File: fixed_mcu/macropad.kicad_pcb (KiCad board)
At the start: 2 copper layers, 92.3 x 115.3 mm, 120 parts, among them J1 USB_C_Receptacle_USB2.0_16P, J2 Conn_01x02, J3 Conn_01x04_Socket, SW1 CherryMX, SW10 CherryMX, SW11 CherryMX, SW12 CherryMX, SW13 CherryMX, SW14 CherryMX, SW15 CherryMX, SW16 CherryMX, SW17 CherryMX, SW18 CherryMX, SW19 CherryMX, SW2 CherryMX, SW20 CherryMX, SW21 SW_Push, SW3 CherryMX, SW4 CherryMX, SW5 CherryMX, SW6 CherryMX, SW7 CherryMX, SW8 CherryMX, SW9 CherryMX, U1 NCP1117-3.3_SOT223, U2 RP2040, U3 SRV05-4, U4 W25Q128JVS, U5 74AHCT1G125, Y1 Crystal_GND24

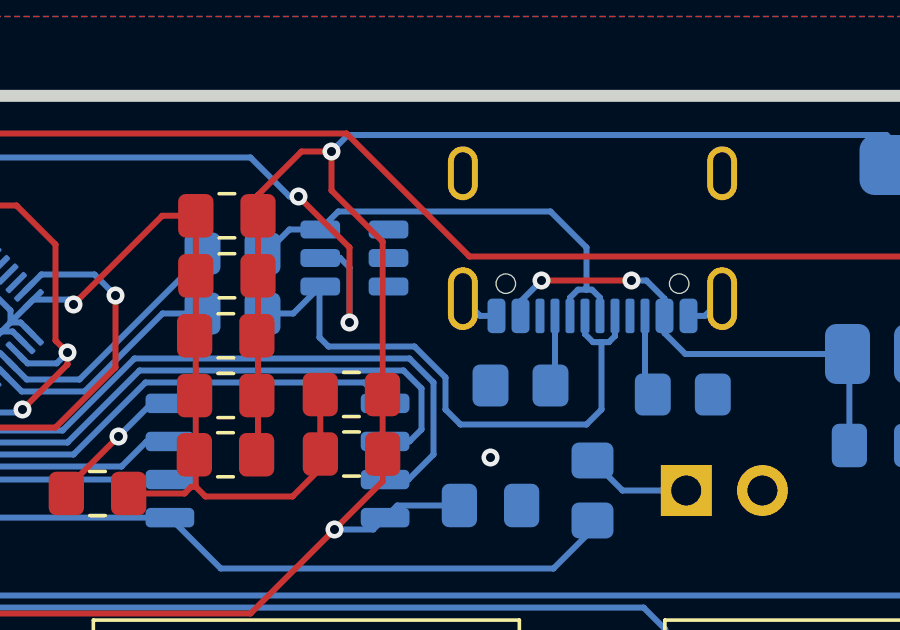
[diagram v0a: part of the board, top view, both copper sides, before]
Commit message: finished modeling enclosures and pad
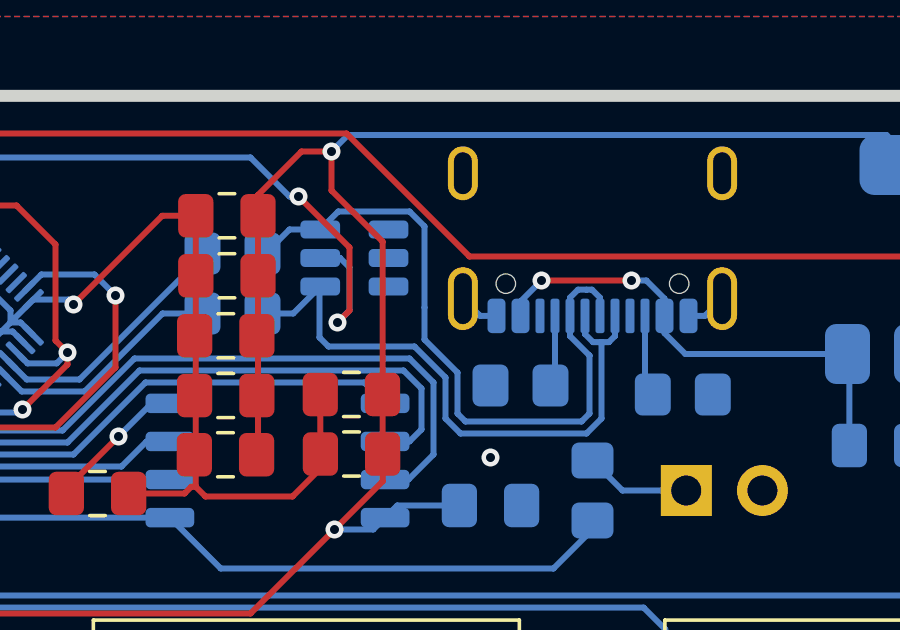
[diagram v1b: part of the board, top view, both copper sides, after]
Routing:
- net /MCU/USB_D-: track 15.8 -> 23.5 mm
- net /MCU/USB_D+: track 20.2 -> 20.8 mm
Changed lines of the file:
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@@
-	)
-	(segment
-		(start 71.9 47.3)
-		(end 73.6 49)
-		(width 0.2)
-		(layer "F.Cu")
-		(net "+5V")
 	)
 	(segment
@@
 	)
 	(segment
+		(start 73.6 49)
+		(end 71.9 47.3)
+		(width 0.2)
+		(layer "F.Cu")
+		(net "+5V")
+	)
+	(segment
+		(start 73.2 51.5)
+		(end 73.6 51.1)
+		(width 0.2)
+		(layer "F.Cu")
+		(net "+5V")
+	)
+	(segment
 		(start 54.9 97.2)
 		(end 73.9 97.2)
@@
 	)
 	(segment
-		(start 73.6 49)
-		(end 73.6 51.5)
-		(width 0.2)
-		(layer "F.Cu")
-		(net "+5V")
-	)
-	(segment
 		(start 54.8 135.3)
 		(end 46.1 135.3)
@@
 		(net "+5V")
 	)
+	(segment
+		(start 73.6 51.1)
+		(end 73.6 49)
+		(width 0.2)
+		(layer "F.Cu")
+		(net "+5V")
+	)
 	(via
 		(at 92.8 135.3)
@@
 	)
 	(via
-		(at 73.6 51.5)
+		(at 73.2 51.5)
 		(size 0.6)
 		(drill 0.3)
@@
 		(drill 0.3)
 		(layers "F.Cu" "B.Cu")
+		(net "+5V")
+	)
+	(segment
+		(start 73.287499 49.35)
+		(end 72.625 49.35)
+		(width 0.2)
+		(layer "B.Cu")
 		(net "+5V")
 	)
@@
 	)
 	(segment
+		(start 73.6 51.1)
+		(end 73.6 49.662501)
+		(width 0.2)
+		(layer "B.Cu")
+		(net "+5V")
+	)
+	(segment
 		(start 74.8875 150.55)
 		(end 74.8875 151.1125)
@@
 	(segment
 		(start 73.6 49.662501)
-		(end 73.6 51.5)
+		(end 73.287499 49.35)
 		(width 0.2)
 		(layer "B.Cu")
@@
 	)
 	(segment
+		(start 73.2 51.5)
+		(end 73.6 51.1)
+		(width 0.2)
+		(layer "B.Cu")
+		(net "+5V")
+	)
+	(segment
 		(start 92.35 77.55)
 		(end 92.35 76.7)
@@
 	)
 	(segment
-		(start 72.625 49.35)
-		(end 73.287499 49.35)
-		(width 0.2)
-		(layer "B.Cu")
-		(net "+5V")
-	)
-	(segment
 		(start 92.25 115.65)
 		(end 92.25 114.8)
@@
 	)
 	(segment
-		(start 73.287499 49.35)
-		(end 73.6 49.662501)
-		(width 0.2)
-		(layer "B.Cu")
-		(net "+5V")
-	)
-	(segment
 		(start 112.9875 93.9625)
 		(end 111.3 95.65)
@@
 	)
 	(segment
+		(start 75.765686 52.3)
+		(end 72.9 52.3)
+		(width 0.2)
+		(layer "B.Cu")
+		(net "/MCU/USB_D+")
+	)
+	(segment
 		(start 81.45 51.88741)
 		(end 81.71759 52.155)
@@
 	)
 	(segment
-		(start 82 54.4)
-		(end 81.5 54.9)
-		(width 0.2)
-		(layer "B.Cu")
-		(net "/MCU/USB_D+")
-	)
-	(segment
-		(start 75.765686 52.3)
-		(end 72.9 52.3)
-		(width 0.2)
-		(layer "B.Cu")
-		(net "/MCU/USB_D+")
-	)
-	(segment
-		(start 76.8 54.4)
-		(end 76.8 53.334314)
-		(width 0.2)
-		(layer "B.Cu")
-		(net "/MCU/USB_D+")
-	)
-	(segment
 		(start 82.245 52.155)
 		(end 82.45 51.95)
@@
 	)
 	(segment
-		(start 82 52.155)
-		(end 82 54.4)
-		(width 0.2)
-		(layer "B.Cu")
-		(net "/MCU/USB_D+")
-	)
-	(segment
-		(start 81.5 54.9)
-		(end 77.3 54.9)
+		(start 76.8 54.7)
+		(end 76.8 53.334314)
+		(width 0.2)
+		(layer "B.Cu")
+		(net "/MCU/USB_D+")
+	)
+	(segment
+		(start 82 54.7)
+		(end 81.5 55.2)
 		(width 0.2)
 		(layer "B.Cu")
@@
 	)
 	(segment
+		(start 82 52.155)
+		(end 82 54.7)
+		(width 0.2)
+		(layer "B.Cu")
+		(net "/MCU/USB_D+")
+	)
+	(segment
+		(start 72.6 52)
+		(end 72.6 50.325)
+		(width 0.2)
+		(layer "B.Cu")
+		(net "/MCU/USB_D+")
+	)
+	(segment
+		(start 82 52.155)
+		(end 82.245 52.155)
+		(width 0.2)
+		(layer "B.Cu")
+		(net "/MCU/USB_D+")
+	)
+	(segment
+		(start 72.6 50.325)
+		(end 72.625 50.3)
+		(width 0.2)
+		(layer "B.Cu")
+		(net "/MCU/USB_D+")
+	)
+	(segment
 		(start 72.9 52.3)
 		(end 72.6 52)
@@
 	)
 	(segment
-		(start 82 52.155)
-		(end 82.245 52.155)
-		(width 0.2)
-		(layer "B.Cu")
-		(net "/MCU/USB_D+")
-	)
-	(segment
-		(start 77.3 54.9)
-		(end 76.8 54.4)
+		(start 81.5 55.2)
+		(end 77.3 55.2)
+		(width 0.2)
+		(layer "B.Cu")
+		(net "/MCU/USB_D+")
+	)
+	(segment
+		(start 76.8 53.334314)
+		(end 75.765686 52.3)
 		(width 0.2)
 		(layer "B.Cu")
@@
 	)
 	(segment
-		(start 72.6 50.325)
-		(end 72.625 50.3)
-		(width 0.2)
-		(layer "B.Cu")
-		(net "/MCU/USB_D+")
-	)
-	(segment
-		(start 76.8 53.334314)
-		(end 75.765686 52.3)
-		(width 0.2)
-		(layer "B.Cu")
-		(net "/MCU/USB_D+")
-	)
-	(segment
 		(start 81.71759 52.155)
 		(end 82 52.155)
@@
 	)
 	(segment
+		(start 77.3 55.2)
+		(end 76.8 54.7)
+		(width 0.2)
+		(layer "B.Cu")
+		(net "/MCU/USB_D+")
+	)
+	(segment
 		(start 70.7 51.2)
 		(end 71.725 51.2)
@@
 	)
 	(segment
-		(start 72.6 52)
-		(end 72.6 50.325)
-		(width 0.2)
-		(layer "B.Cu")
-		(net "/MCU/USB_D+")
-	)
-	(segment
 		(start 81.45 51.28)
 		(end 81.45 51.88741)
@@
 	)
 	(segment
-		(start 81.5 49)
-		(end 81.5 50.405)
-		(width 0.2)
-		(layer "B.Cu")
-		(net "/MCU/USB_D-")
-	)
-	(segment
 		(start 81.21759 50.405)
 		(end 81.5 50.405)
@@
 	)
 	(segment
+		(start 81.334314 54.8)
+		(end 77.465686 54.8)
+		(width 0.2)
+		(layer "B.Cu")
+		(net "/MCU/USB_D-")
+	)
+	(segment
 		(start 81.68241 50.405)
 		(end 81.95 50.67259)
@@
 	)
 	(segment
+		(start 73.225 47.8)
+		(end 72.625 48.4)
+		(width 0.2)
+		(layer "B.Cu")
+		(net "/MCU/USB_D-")
+	)
+	(segment
 		(start 70.7 49.3)
 		(end 71.6 48.4)
@@
 	)
 	(segment
+		(start 81.6 52.6)
+		(end 81.6 54.534314)
+		(width 0.2)
+		(layer "B.Cu")
+		(net "/MCU/USB_D-")
+	)
+	(segment
 		(start 80.95 51.28)
 		(end 80.95 50.67259)
@@
 	)
 	(segment
-		(start 72.625 48.4)
+		(start 77.2 54.534314)
+		(end 77.2 53.168628)
+		(width 0.2)
+		(layer "B.Cu")
+		(net "/MCU/USB_D-")
+	)
+	(segment
+		(start 76.1 51)
+		(end 76.1 48.296948)
+		(width 0.2)
+		(layer "B.Cu")
+		(net "/MCU/USB_D-")
+	)
+	(segment
+		(start 81.596905 52.6)
+		(end 81.6 52.6)
+		(width 0.2)
+		(layer "B.Cu")
+		(net "/MCU/USB_D-")
+	)
+	(segment
+		(start 75.603052 47.8)
 		(end 73.225 47.8)
+		(width 0.2)
+		(layer "B.Cu")
+		(net "/MCU/USB_D-")
+	)
+	(segment
+		(start 77.465686 54.8)
+		(end 77.2 54.534314)
 		(width 0.2)
 		(layer "B.Cu")
@@
 	)
 	(segment
-		(start 80.3 47.8)
-		(end 81.5 49)
+		(start 81.6 54.534314)
+		(end 81.334314 54.8)
 		(width 0.2)
 		(layer "B.Cu")
@@
 	)
 	(segment
-		(start 73.225 47.8)
-		(end 80.3 47.8)
-		(width 0.2)
-		(layer "B.Cu")
+		(start 80.95 51.953095)
+		(end 81.596905 52.6)
+		(width 0.2)
+		(layer "B.Cu")
+		(net "/MCU/USB_D-")
+	)
+	(segment
+		(start 77.2 53.168628)
+		(end 76.1 52.068628)
+		(width 0.2)
+		(layer "B.Cu")
+		(net "/MCU/USB_D-")
+	)
+	(segment
+		(start 80.95 51.28)
+		(end 80.95 51.953095)
+		(width 0.2)
+		(layer "B.Cu")
+		(net "/MCU/USB_D-")
+	)
+	(segment
+		(start 76.1 52.068628)
+		(end 76.1 51)
+		(width 0.2)
+		(layer "B.Cu")
+		(net "/MCU/USB_D-")
+	)
+	(segment
+		(start 76.1 48.296948)
+		(end 75.603052 47.8)
+		(width 0.2)
+		(layer "B.Cu")
